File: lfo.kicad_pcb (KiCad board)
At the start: 2 copper layers, 103.7 x 33.7 mm, 43 parts, among them J1 PJ398SM-12 (Tri), J2 PJ398SM-12 (square), J3 PJ398SM-12 (weird), J4 Conn_02x05_Odd_Even, Q1 BC547, SW1 SW_SPDT, U1 TL084

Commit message: add mounting hole
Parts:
- moved C4 10.2 mm to (143.2, 38.1), turned to -90 degrees
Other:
- outline, holes or cut-outs redrawn
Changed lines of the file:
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@@
 		(allow_soldermask_bridges_in_footprints no)
 		(tenting front back)
+		(aux_axis_origin 147.9 27.55)
 		(pcbplotparams
 			(layerselection 0x00000000_00000000_55555555_5755f5ff)
@@
 	(footprint "Capacitor_THT:C_Disc_D4.7mm_W2.5mm_P5.00mm"
 		(layer "F.Cu")
-		(at 148.6 29.5 90)
+		(at 143.15 38.1 -90)
 		(descr "C, Disc series, Radial, pin pitch=5.00mm, diameter*width=4.7*2.5mm^2, Capacitor, http://www.vishay.com/docs/45233/krseries.pdf")
 		(tags "C Disc series Radial pin pitch 5.00mm diameter 4.7mm width 2.5mm Capacitor")
@@
 		(attr through_hole)
 		(fp_line
-			(start 4.97 -1.37)
-			(end 4.97 -1.04)
+			(start 0.03 1.37)
+			(end 4.97 1.37)
 			(stroke
 				(width 0.12)
@@
 		)
 		(fp_line
-			(start 0.03 -1.37)
-			(end 4.97 -1.37)
+			(start 0.03 1.04)
+			(end 0.03 1.37)
 			(stroke
 				(width 0.12)
@@
 		)
 		(fp_line
-			(start 0.03 -1.37)
-			(end 0.03 -1.04)
+			(start 4.97 1.04)
+			(end 4.97 1.37)
 			(stroke
 				(width 0.12)
@@
 		)
 		(fp_line
-			(start 4.97 1.04)
-			(end 4.97 1.37)
+			(start 0.03 -1.37)
+			(end 0.03 -1.04)
 			(stroke
 				(width 0.12)
@@
 		)
 		(fp_line
-			(start 0.03 1.04)
-			(end 0.03 1.37)
+			(start 0.03 -1.37)
+			(end 4.97 -1.37)
 			(stroke
 				(width 0.12)
@@
 		)
 		(fp_line
-			(start 0.03 1.37)
-			(end 4.97 1.37)
+			(start 4.97 -1.37)
+			(end 4.97 -1.04)
 			(stroke
 				(width 0.12)
@@
 		)
 		(fp_line
-			(start 6.05 -1.5)
-			(end -1.05 -1.5)
+			(start -1.05 1.5)
+			(end 6.05 1.5)
 			(stroke
 				(width 0.05)
@@
 		)
 		(fp_line
-			(start -1.05 -1.5)
-			(end -1.05 1.5)
+			(start 6.05 1.5)
+			(end 6.05 -1.5)
 			(stroke
 				(width 0.05)
@@
 		)
 		(fp_line
-			(start 6.05 1.5)
-			(end 6.05 -1.5)
+			(start -1.05 -1.5)
+			(end -1.05 1.5)
 			(stroke
 				(width 0.05)
@@
 		)
 		(fp_line
-			(start -1.05 1.5)
-			(end 6.05 1.5)
+			(start 6.05 -1.5)
+			(end -1.05 -1.5)
 			(stroke
 				(width 0.05)
@@
 		)
 		(fp_line
-			(start 4.85 -1.25)
-			(end 0.15 -1.25)
+			(start 0.15 1.25)
+			(end 4.85 1.25)
 			(stroke
 				(width 0.1)
@@
 		)
 		(fp_line
-			(start 0.15 -1.25)
-			(end 0.15 1.25)
+			(start 4.85 1.25)
+			(end 4.85 -1.25)
 			(stroke
 				(width 0.1)
@@
 		)
 		(fp_line
-			(start 4.85 1.25)
-			(end 4.85 -1.25)
+			(start 0.15 -1.25)
+			(end 0.15 1.25)
 			(stroke
 				(width 0.1)
@@
 		)
 		(fp_line
-			(start 0.15 1.25)
-			(end 4.85 1.25)
+			(start 4.85 -1.25)
+			(end 0.15 -1.25)
 			(stroke
 				(width 0.1)
@@
 		)
 		(pad "1" thru_hole circle
-			(at 0 0 90)
+			(at 0 0 270)
 			(size 1.6 1.6)
 			(drill 0.8)
@@
 		)
 		(pad "2" thru_hole circle
-			(at 5 0 90)
+			(at 5 0 270)
 			(size 1.6 1.6)
 			(drill 0.8)
@@
 		(layer "Edge.Cuts")
 	)
+	(gr_circle
+		(center 147.5 28.05)
+		(end 149.45 28.6)
+		(stroke
+			(width 0.1)
+			(type default)
+		)
+		(fill no)
+		(layer "Edge.Cuts")
+	)

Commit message: routing update
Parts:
- removed the R4 at (107.0, 41.8)
- D4: footprint Diode_THT:D_DO-201AD_P3.81mm_Vertical_AnodeUp -> Diode_THT:D_DO-41_SOD81_P10.16mm_Horizontal
- moved R15 32.3 mm to (128.2, 34.1), turned to -90 degrees
- moved D3 23.3 mm to (153.8, 17.6), turned to 0 degrees
- moved D4 22.4 mm to (156.6, 40.6)
- moved R2 13.0 mm to (117.7, 43.2), turned to 0 degrees
- moved R14 11.0 mm to (116.4, 28.1), turned to 180 degrees
- moved R5 7.40 mm to (74.8, 34.0)
- moved R7 4.99 mm to (106.0, 39.0), turned to 180 degrees
- moved R3 3.16 mm to (97.2, 31.8)
- moved C3 0.86 mm to (146.6, 38.2), turned to 0 degrees
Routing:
- net Net-(SW1-B): track 15.8 -> 96.6 mm
- net Vcc: track 0.00 -> 78.3 mm
- net Vee: track 0.00 -> 70.1 mm, vias 0 -> 1
- net GND: track 169.2 -> 214.2 mm
- net Net-(SW1-C): track 0.00 -> 36.2 mm
- net Net-(R13-Pad2): track 0.00 -> 31.2 mm, vias 0 -> 1
- net Net-(C1-Pad2): track 41.0 -> 69.1 mm, vias 0 -> 1
- net Net-(R15-Pad2): track 83.9 -> 111.5 mm
- net Net-(Q1-C): track 12.9 -> 33.0 mm
- net Net-(D1-A): track 6.18 -> 22.9 mm
- net Net-(J2-PadT): track 43.7 -> 56.9 mm
- net Net-(D3-A): track 0.00 -> 9.51 mm
- net Net-(D4-K): track 0.00 -> 8.85 mm
- net Net-(U1B-+): track 0.00 -> 8.12 mm, vias 0 -> 1
- net Net-(D1-K): track 26.3 -> 32.0 mm
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
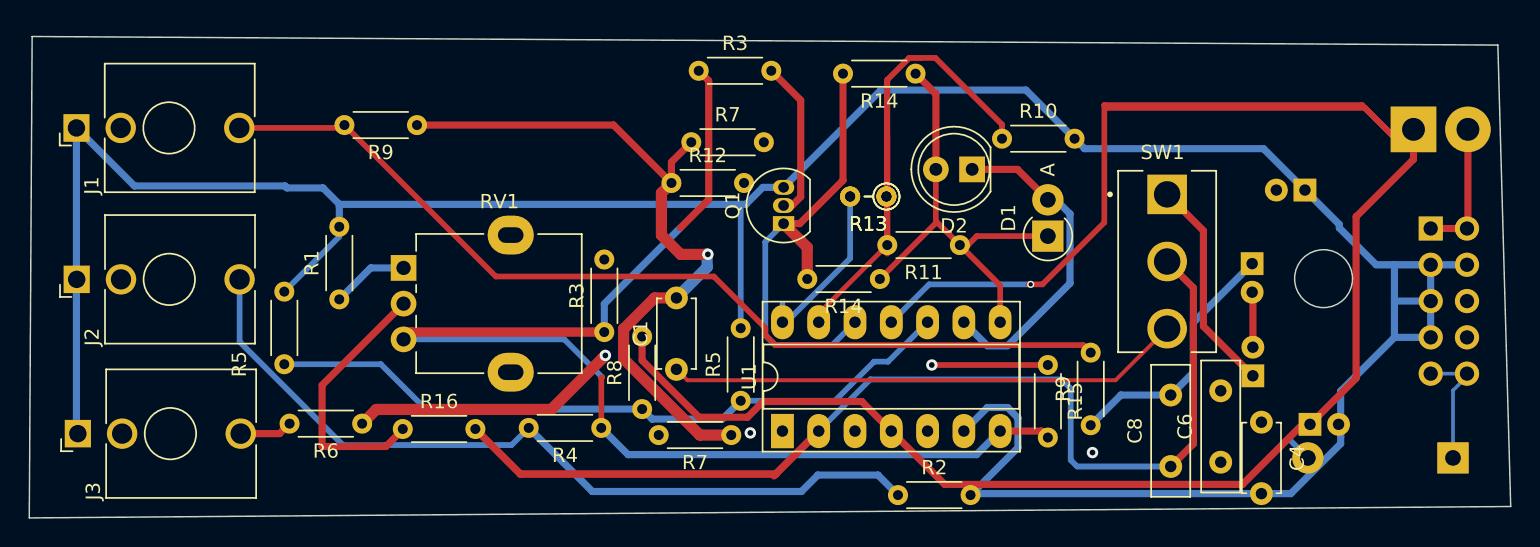
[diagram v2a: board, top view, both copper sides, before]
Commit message: remove redundant components
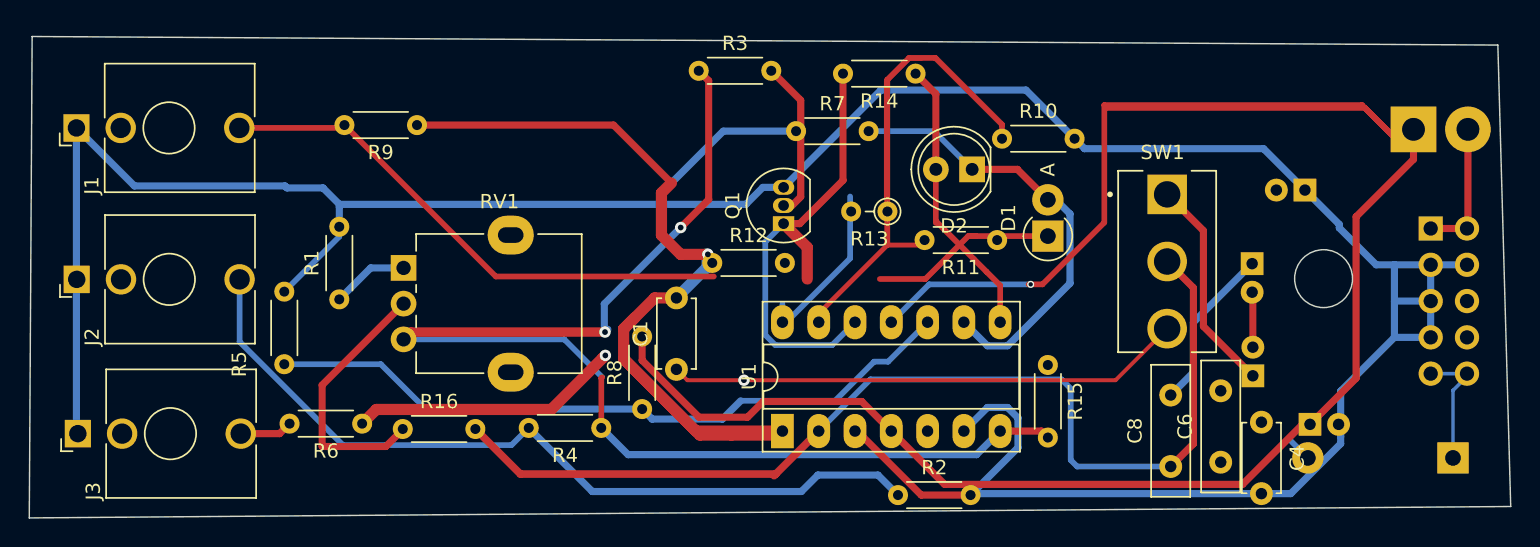
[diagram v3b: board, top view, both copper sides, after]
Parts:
- removed the R13 at (116.9, 22.3)
- removed the R14 at (116.4, 28.1)
- removed the R3 at (97.2, 31.8)
- removed the R5 at (106.7, 36.6)
- removed the R7 at (106.0, 39.0)
- removed the R9 at (131.2, 38.3)
- moved R7 7.38 mm to (110.6, 17.7)
- moved R12 6.28 mm to (104.7, 26.9)
- moved R11 2.63 mm to (124.7, 25.4)
- moved R13 1.05 mm to (117.0, 23.4)
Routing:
- net Net-(J1-PadT): track 66.6 -> 37.7 mm
- net Net-(C1-Pad2): track 69.1 -> 87.4 mm
- net Net-(D1-A): track 22.9 -> 31.3 mm
- net Net-(U1B-+): track 8.12 -> 0.00 mm, vias 1 -> 0
- net Net-(U1D--): track 53.5 -> 48.0 mm
- net Net-(D1-K): track 32.0 -> 33.5 mm
- net GND: track 214.2 -> 215.5 mm
- net Net-(SW1-C): vias 0 -> 1
- net Net-(R15-Pad2): vias 0 -> 2
- net (no net): vias 2 -> 0

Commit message: successcive editing
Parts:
- removed C6: 100nFC, Capacitor_THT:C_Disc_D9.0mm_W2.5mm_P5.00mm
- moved R15 22.4 mm to (105.8, 34.2)
- moved C8 6.85 mm to (131.6, 36.8), turned to 0 degrees
- moved C1 5.48 mm to (98.6, 30.2)
- moved R12 2.35 mm to (106.9, 26.1), turned to -90 degrees
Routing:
- net Vee: track 70.1 -> 98.9 mm
- net Net-(U1B-+): track 0.00 -> 24.3 mm, vias 0 -> 1
- net Net-(C1-Pad2): track 87.4 -> 103.0 mm, vias 1 -> 2
- net Net-(J1-PadT): track 37.7 -> 22.4 mm
- net Net-(R13-Pad2): track 31.2 -> 44.6 mm, vias 1 -> 2
- net Net-(D1-K): track 33.5 -> 25.8 mm
- net Net-(SW1-B): track 96.6 -> 103.7 mm, vias 0 -> 3
- net GND: track 215.5 -> 222.1 mm
- net Net-(SW1-C): track 36.2 -> 42.7 mm, vias 1 -> 0
- net Net-(Q1-C): track 33.0 -> 28.5 mm
- net Vcc: track 78.3 -> 80.9 mm
- net Net-(R15-Pad2): track 111.5 -> 109.5 mm
- net Net-(J2-PadT): track 56.9 -> 55.9 mm

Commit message: fix drc errors
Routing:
- net Net-(SW1-C): track 42.7 -> 96.1 mm
- net Vee: track 98.9 -> 74.6 mm
- net Net-(C1-Pad2): track 103.0 -> 121.9 mm, vias 2 -> 4
- net Net-(J1-PadT): track 22.4 -> 7.44 mm
- net GND: track 222.1 -> 233.4 mm
- net Net-(Q1-B): track 11.1 -> 12.2 mm
- net Net-(R15-Pad2): vias 2 -> 4

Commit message: furter chnges
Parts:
- removed C8: 470pFC, Capacitor_THT:C_Disc_D9.0mm_W2.5mm_P5.00mm
- D4: footprint Diode_THT:D_DO-41_SOD81_P10.16mm_Horizontal -> Diode_THT:D_DO-201AD_P3.81mm_Vertical_AnodeUp
- moved R2 5.44 mm to (112.3, 43.1)
- moved R10 3.00 mm to (123.0, 16.1)
- moved R12 2.60 mm to (104.3, 26.2)
- moved R8 1.91 mm to (99.8, 39.1)
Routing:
- net Vee: track 74.6 -> 55.1 mm, vias 1 -> 2
- net Net-(J2-PadT): track 55.9 -> 51.1 mm
- net Net-(U1D--): track 48.0 -> 46.3 mm
- net Vcc: track 80.9 -> 79.2 mm
- net Net-(U1C-+): track 49.7 -> 51.3 mm
- net Net-(U1B-+): track 24.3 -> 25.7 mm
- net GND: track 233.4 -> 234.7 mm
- net Net-(C1-Pad2): track 121.9 -> 121.2 mm

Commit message: finalize
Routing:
- net Vee: track 55.1 -> 71.4 mm
- net Net-(C1-Pad2): track 121.2 -> 121.9 mm, vias 4 -> 2
- net Net-(R15-Pad2): track 109.5 -> 109.4 mm, vias 4 -> 3
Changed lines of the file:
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@@
+	)
+	(segment
+		(start 132.111883 22.538117)
+		(end 135.05 19.6)
+		(width 0.4)
+		(layer "F.Cu")
+		(net 2)
+	)
+	(segment
+		(start 142.75 19.6)
+		(end 142.75 20.405112)
+		(width 0.4)
+		(layer "F.Cu")
+		(net 2)
 	)
 	(segment
@@
 	)
 	(segment
+		(start 132.111883 24.161883)
+		(end 127.823766 28.45)
+		(width 0.4)
+		(layer "F.Cu")
+		(net 2)
+	)
+	(segment
 		(start 150.195 15.9)
 		(end 149.013518 15.9)
@@
 	)
 	(segment
+		(start 142.75 20.405112)
+		(end 144.194888 21.85)
+		(width 0.4)
+		(layer "F.Cu")
+		(net 2)
+	)
+	(segment
 		(start 132.15 24.123766)
-		(end 127.823766 28.45)
+		(end 132.111883 24.161883)
 		(width 0.4)
 		(layer "F.Cu")
@@
 	)
 	(segment
+		(start 132.111883 24.161883)
+		(end 132.111883 22.538117)
+		(width 0.4)
+		(layer "F.Cu")
+		(net 2)
+	)
+	(segment
 		(start 127.823766 28.45)
 		(end 127 28.45)
+		(width 0.4)
+		(layer "F.Cu")
+		(net 2)
+	)
+	(segment
+		(start 135.05 19.6)
+		(end 142.75 19.6)
 		(width 0.4)
 		(layer "F.Cu")
@@
 	)
 	(via
-		(at 104.4 26.35)
-		(size 0.8)
-		(drill 0.4)
-		(layers "F.Cu" "B.Cu")
-		(net 5)
-	)
-	(via
 		(at 101.91198 21.29198)
 		(size 0.8)
@@
 		(net 5)
 	)
-	(via
-		(at 101.850964 21.352995)
-		(size 0.8)
-		(drill 0.4)
-		(layers "F.Cu" "B.Cu")
-		(net 5)
-	)
 	(segment
 		(start 105.478959 17.725)
@@
 	)
 	(segment
+		(start 136.55 36.45)
+		(end 136.55 36.8)
+		(width 0.5)
+		(layer "B.Cu")
+		(net 5)
+	)
+	(segment
 		(start 130.81611 34.09611)
 		(end 133.52 36.8)
@@
 		(end 112.9 35.775)
 		(width 0.7834)
+		(layer "B.Cu")
+		(net 5)
+	)
+	(segment
+		(start 138.3885 34.6115)
+		(end 136.55 36.45)
+		(width 0.5)
 		(layer "B.Cu")
 		(net 5)
@@
 	)
 	(segment
-		(start 138.3885 34.6115)
-		(end 136.8 36.2)
-		(width 0.5)
-		(layer "B.Cu")
-		(net 5)
-	)
-	(segment
 		(start 109.62 38.72)
 		(end 109.790425 38.72)
@@
 		(start 102.4975 24.4725)
 		(end 102.47 24.5)
-		(width 0.5)
-		(layer "F.Cu")
-		(net 9)
-	)
-	(segment
-		(start 102.545 24.425)
-		(end 102.4975 24.4725)
 		(width 0.5)
 		(layer "F.Cu")
@@
 		(size 0.8)
 		(drill 0.4)
-		(layers "F.Cu" "B.Cu")
-		(net 9)
-	)
-	(via
-		(at 102.545 24.425)
-		(size 0.8)
-		(drill 0.4)

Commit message: finalize (2)
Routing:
- net Net-(SW1-C): track 96.1 -> 75.2 mm
- net Net-(C1-Pad2): track 121.9 -> 106.9 mm
- net Vee: track 71.4 -> 60.6 mm
- net Net-(SW1-B): track 103.7 -> 108.0 mm, vias 3 -> 2
- net Net-(U1B-+): track 25.7 -> 24.4 mm
- net Net-(R13-Pad2): track 44.7 -> 43.7 mm
- net Net-(U1D--): track 46.3 -> 45.4 mm
